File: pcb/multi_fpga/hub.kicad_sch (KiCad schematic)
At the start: 6 parts

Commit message: Fixed with real TXO.
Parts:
- Y1: footprint multi_fpga:TCXO_Can -> multi_fpga:ECS-TXO-5032-122.8-TR
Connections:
- net +3V3: now also Y1.4 (VDD); no longer Y1.1 (VDD), Y1.3 (OE)
- net TCXO_CLK: now also Y1.3 (OUTPUT); no longer Y1.4 (OUT)
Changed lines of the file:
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@@
-	(wire
-		(pts
-			(xy 332.74 185.42) (xy 322.58 185.42)
-		)
-		(stroke
-			(width 0)
-			(type default)
-		)
-	)
 	(wire
 		(pts
@@
 	)
 	(symbol
-		(lib_id "power:+3V3")
-		(at 322.58 185.42 0)
-		(unit 1)
-		(body_style 1)
-		(exclude_from_sim no)
-		(in_bom yes)
-		(on_board yes)
-		(in_pos_files yes)
-		(dnp no)
-		(property "Reference" "#PWR0521"
-			(at 322.58 185.42 0)
-			(hide yes)
-			(show_name no)
-			(do_not_autoplace no)
-			(effects
-				(font
-					(size 1.27 1.27)
-				)
-			)
-		)
-		(property "Value" "+3V3"
-			(at 322.58 185.42 0)
-			(hide yes)
-			(show_name no)
-			(do_not_autoplace no)
-			(effects
-				(font
-					(size 1.27 1.27)
-				)
-			)
-		)
-		(property "Footprint" ""
-			(at 322.58 185.42 0)
-			(hide yes)
-			(show_name no)
-			(do_not_autoplace no)
-			(effects
-				(font
-					(size 1.27 1.27)
-				)
-			)
-		)
-		(property "Datasheet" ""
-			(at 322.58 185.42 0)
-			(hide yes)
-			(show_name no)
-			(do_not_autoplace no)
-			(effects
-				(font
-					(size 1.27 1.27)
-				)
-			)
-		)
-		(property "Description" ""
-			(at 322.58 185.42 0)
-			(hide yes)
-			(show_name no)
-			(do_not_autoplace no)
-			(effects
-				(font
-					(size 1.27 1.27)
-				)
-			)
-		)
-		(pin "1"
-		)
-		(instances
-			(project "hub"
-				(path "/47ab59f9-efc4-4196-ab70-a13d317b89f4"
-					(reference "#PWR0521")
-					(unit 1)
-				)
-			)
-			(project "top"
-				(path "/80f109c4-96c5-4385-bfb6-0f7a96b014ab/a20cffda-dc30-4756-aadc-e7b7a5015c1f"
-					(reference "#PWR0521")
-					(unit 1)
-				)
-			)
-		)
-	)
-	(symbol
 		(lib_id "C")
 		(at 369.57 233.68 0)
@@
 			)
 		)
-		(property "Footprint" "multi_fpga:TCXO_Can"
+		(property "Footprint" "multi_fpga:ECS-TXO-5032-122.8-TR"
 			(at 350.52 184.15 0)
 			(hide yes)

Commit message: Rotated USB-C connector down. Hand-routed. DRC-clean.
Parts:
- A6: footprint multi_fpga:FT232H_Breakout -> multi_fpga:Adafruit_FT232H
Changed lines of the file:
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@@
 			)
 		)
-		(property "Footprint" "multi_fpga:FT232H_Breakout"
+		(property "Footprint" "multi_fpga:Adafruit_FT232H"
 			(at 350.52 294.64 0)
 			(hide yes)

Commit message: Added/cleaned-up power.
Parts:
- added C3: .1uF, SparkFun-Capacitor:C_0603_1608Metric, symbol SparkFun-Capacitor:C
- added C4: 10uF, SparkFun-Capacitor:C_0603_1608Metric_Polar, symbol SparkFun-Capacitor:10uF_0603_6.3V_20%_Polar(Tant)
- added C5: 100uF, SparkFun-Capacitor:Panasonic_D, symbol SparkFun-Capacitor:100uF_6.6x6.6_25V_20%
- added J1: Cluster00_SpokeBus, Connector_PinSocket_2.54mm:PinSocket_2x06_P2.54mm_Vertical, symbol Connector_Generic:Conn_02x06_Odd_Even
- added J2: Cluster01_SpokeBus, Connector_PinSocket_2.54mm:PinSocket_2x06_P2.54mm_Vertical, symbol Connector_Generic:Conn_02x06_Odd_Even
- added J3: Cluster02_SpokeBus, Connector_PinSocket_2.54mm:PinSocket_2x06_P2.54mm_Vertical, symbol Connector_Generic:Conn_02x06_Odd_Even
- added J4: Cluster03_SpokeBus, Connector_PinSocket_2.54mm:PinSocket_2x06_P2.54mm_Vertical, symbol Connector_Generic:Conn_02x06_Odd_Even
- added J5: Cluster00_Power, Connector_PinSocket_2.54mm:PinSocket_1x02_P2.54mm_Vertical, symbol Connector_Generic:Conn_01x02
- added J6: Cluster01_Power, Connector_PinSocket_2.54mm:PinSocket_1x02_P2.54mm_Vertical, symbol Connector_Generic:Conn_01x02
- added J7: Cluster02_Power, Connector_PinSocket_2.54mm:PinSocket_1x02_P2.54mm_Vertical, symbol Connector_Generic:Conn_01x02
- added J8: Cluster03_Power, Connector_PinSocket_2.54mm:PinSocket_1x02_P2.54mm_Vertical, symbol Connector_Generic:Conn_01x02
- added J9: Main Power Input, Connector_JST:JST_XH_B2B-XH-A_1x02_P2.50mm_Vertical, symbol Connector_Generic:Conn_01x02
- C1, C2: value 100nF -> 1uF; footprint (none) -> Capacitor_SMD:C_0201_0603Metric
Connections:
- net +3V3: now also C3.1
- net +5V: now also C4.1, C5.1, J5.1 (Pin_1), J6.1 (Pin_1), J7.1 (Pin_1), J8.1 (Pin_1), J9.1 (Pin_1)
- net GND: now also C3.2, C4.2, C5.2, J1.11 (Pin_11), J1.12 (Pin_12), J1.5 (Pin_5), J1.6 (Pin_6), J2.11 (Pin_11), J2.12 (Pin_12), J2.5 (Pin_5), J2.6 (Pin_6), J3.11 (Pin_11), J3.12 (Pin_12), J3.5 (Pin_5), J3.6 (Pin_6), J4.11 (Pin_11), J4.12 (Pin_12), J4.5 (Pin_5), J4.6 (Pin_6), J5.2 (Pin_2), J6.2 (Pin_2), J7.2 (Pin_2), J8.2 (Pin_2), J9.2 (Pin_2)
- net SPOKE0_CLK: now also J1.10 (Pin_10)
- net SPOKE0_D0: now also J1.1 (Pin_1)
- net SPOKE0_D1: now also J1.2 (Pin_2)
- net SPOKE0_D2: now also J1.3 (Pin_3)
- net SPOKE0_D3: now also J1.4 (Pin_4)
- net SPOKE0_D4: now also J1.7 (Pin_7)
- net SPOKE0_D5: now also J1.8 (Pin_8)
- net SPOKE0_STROBE: now also J1.9 (Pin_9)
- net SPOKE1_CLK: now also J2.10 (Pin_10)
- net SPOKE1_D0: now also J2.1 (Pin_1)
- net SPOKE1_D1: now also J2.2 (Pin_2)
- net SPOKE1_D2: now also J2.3 (Pin_3)
- net SPOKE1_D3: now also J2.4 (Pin_4)
- net SPOKE1_D4: now also J2.7 (Pin_7)
- net SPOKE1_D5: now also J2.8 (Pin_8)
- net SPOKE1_STROBE: now also J2.9 (Pin_9)
- net SPOKE2_CLK: now also J3.10 (Pin_10)
- net SPOKE2_D0: now also J3.1 (Pin_1)
- net SPOKE2_D1: now also J3.2 (Pin_2)
- net SPOKE2_D2: now also J3.3 (Pin_3)
- net SPOKE2_D3: now also J3.4 (Pin_4)
- net SPOKE2_D4: now also J3.7 (Pin_7)
- net SPOKE2_D5: now also J3.8 (Pin_8)
- net SPOKE2_STROBE: now also J3.9 (Pin_9)
- net SPOKE3_CLK: now also J4.10 (Pin_10)
- net SPOKE3_D0: now also J4.1 (Pin_1)
- net SPOKE3_D1: now also J4.2 (Pin_2)
- net SPOKE3_D2: now also J4.3 (Pin_3)
- net SPOKE3_D3: now also J4.4 (Pin_4)
- net SPOKE3_D4: now also J4.7 (Pin_7)
- net SPOKE3_D5: now also J4.8 (Pin_8)
- net SPOKE3_STROBE: now also J4.9 (Pin_9)
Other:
- moved on the sheet: A5, A6, C1, C2, VR5, Y1

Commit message: Fixed library and power issues.
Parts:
- A5: symbol CMOD_A7_35T -> multi_fpga:CMOD_A7_35T
- A6: symbol FT232H_BRK -> multi_fpga:FT232H_BRK
- C1, C2: symbol C -> multi_fpga:C
- VR5: symbol LDO_3V3 -> Regulator_Linear:MCP1700x-330xxTT
- Y1: symbol TCXO_OSC -> multi_fpga:TCXO_OSC
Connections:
- net +3V3: no longer VR5.2 (OUT)
- net +5V: no longer VR5.3 (IN)
- net GND: no longer VR5.1 (GND)
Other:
- moved on the sheet: VR5
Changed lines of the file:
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@@
 	)
 	(symbol
-		(lib_id "C")
+		(lib_id "multi_fpga:C")
 		(at 482.6 146.05 0)
 		(unit 1)
@@
 	)
 	(symbol
-		(lib_id "CMOD_A7_35T")
+		(lib_id "multi_fpga:CMOD_A7_35T")
 		(at 400.05 171.45 0)
 		(unit 1)
@@
 	)
 	(symbol
-		(lib_id "C")
+		(lib_id "multi_fpga:C")
 		(at 497.84 156.21 0)
 		(unit 1)
@@
 	)
 	(symbol
-		(lib_id "TCXO_OSC")
+		(lib_id "multi_fpga:TCXO_OSC")
 		(at 525.78 204.47 0)
 		(unit 1)
@@
 	)
 	(symbol
-		(lib_id "FT232H_BRK")
+		(lib_id "multi_fpga:FT232H_BRK")
 		(at 334.01 345.44 0)
 		(unit 1)
@@
 	)
 	(symbol
-		(lib_id "LDO_3V3")
+		(lib_id "Regulator_Linear:MCP1700x-330xxTT")
 		(at 524.51 139.7 0)
 		(unit 1)
@@
 		)
 	)
-	(embedded_fonts no)
 )

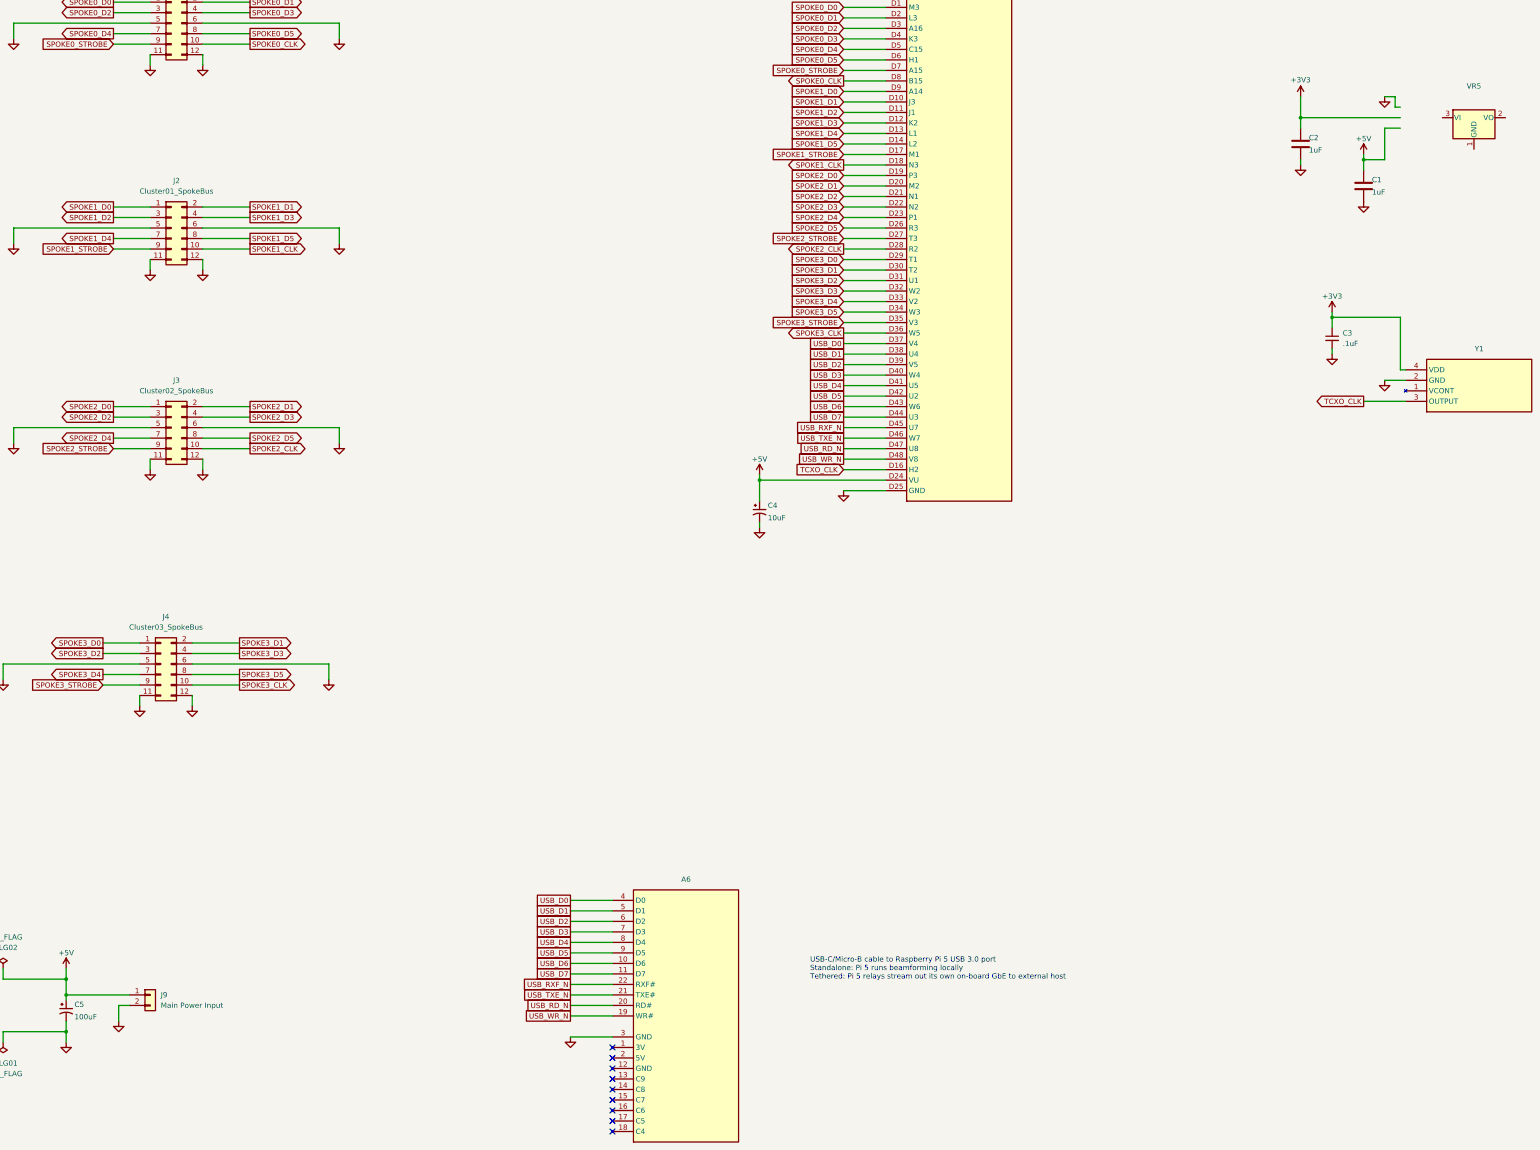
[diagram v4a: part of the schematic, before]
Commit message: Fixed power and C ref des collisions.
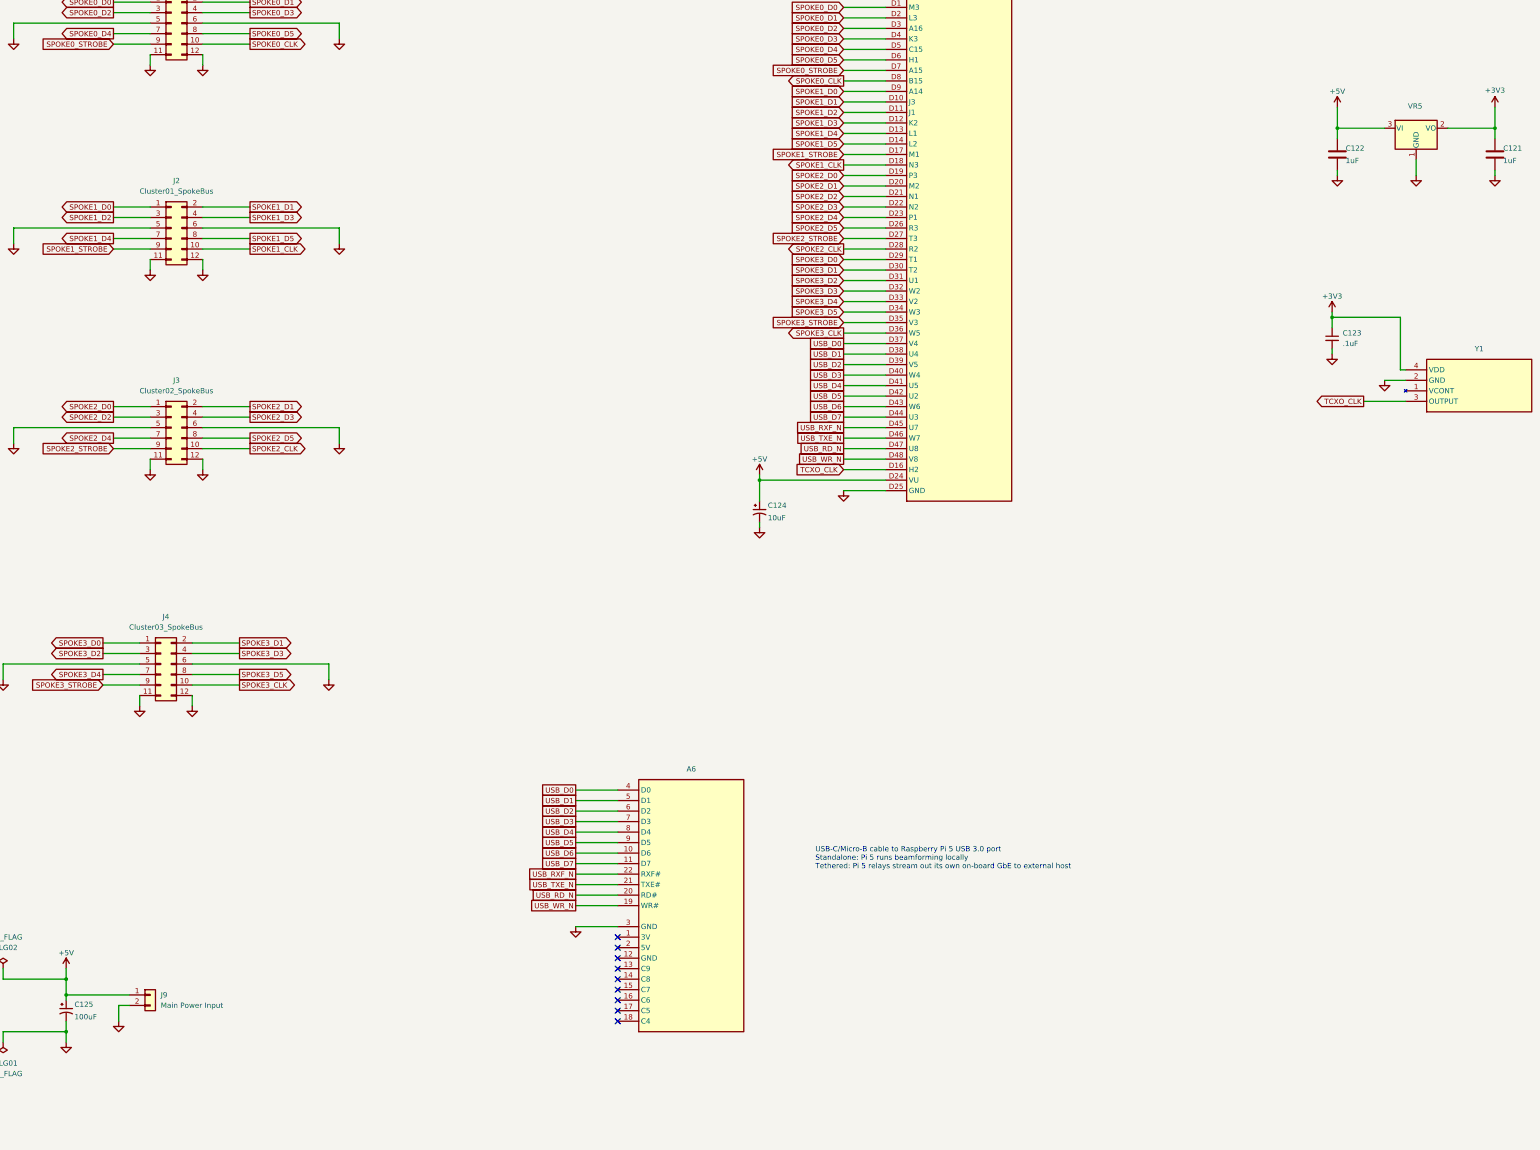
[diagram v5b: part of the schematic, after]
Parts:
- renumbered C2 to C121, C1 to C122, C3 to C123, C4 to C124, C5 to C125
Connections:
- net +3V3: now also VR5.2 (VO)
- net +5V: now also VR5.3 (VI)
- net GND: now also VR5.1 (GND)
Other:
- moved on the sheet: A6, C121, C122, VR5

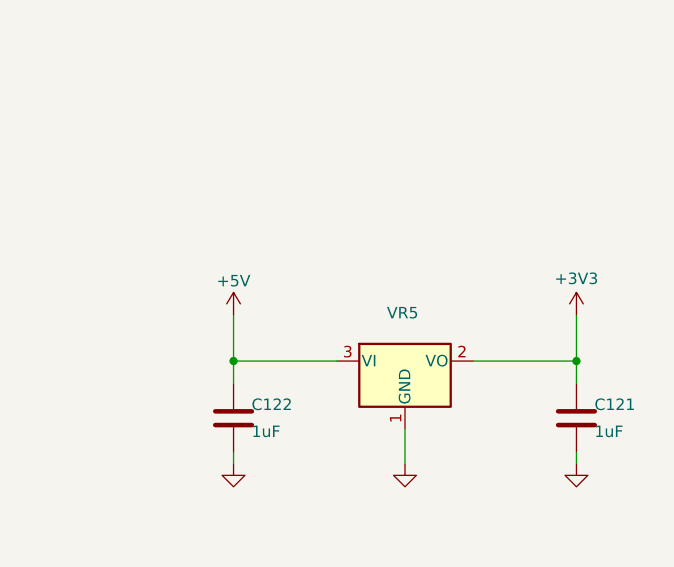
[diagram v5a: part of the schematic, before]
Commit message: Added the LDO regulator part numbers.
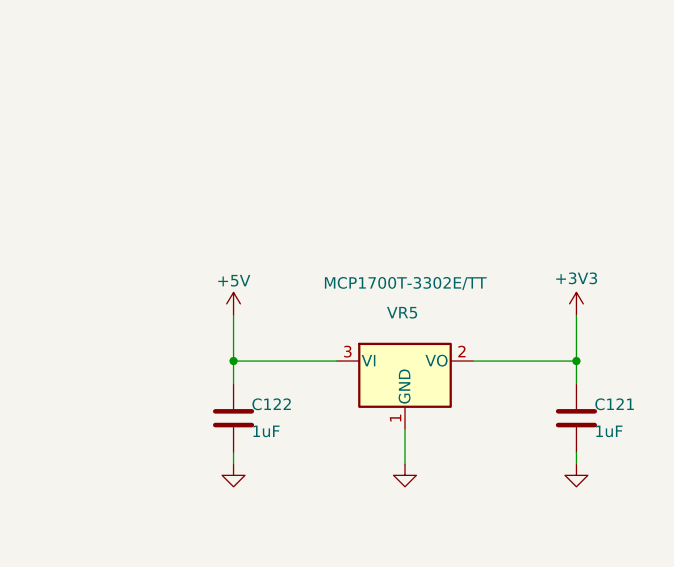
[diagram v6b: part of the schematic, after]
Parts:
- VR5: value (none) -> MCP1700T-3302E/TT
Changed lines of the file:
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@@
 			)
 		)
-		(property "Value" ""
-			(at 510.54 142.24 0)
+		(property "Value" "MCP1700T-3302E/TT"
+			(at 510.54 133.604 0)
 			(show_name no)
 			(do_not_autoplace no)
@@
 		)
 	)
+	(embedded_fonts no)
 )

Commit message: Fixed FPGA module symbols.
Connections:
- net +5V: now also A5.24 (VU); no longer A5.D24 (VU)
- net GND: now also A5.25 (GND); no longer A5.D25 (GND)
- net SPOKE0_CLK: now also A5.8 (PIO08); no longer A5.D8 (B15)
- net SPOKE0_D0: now also A5.1 (PIO01); no longer A5.D1 (M3)
- net SPOKE0_D1: now also A5.2 (PIO02); no longer A5.D2 (L3)
- net SPOKE0_D2: now also A5.3 (PIO03); no longer A5.D3 (A16)
- net SPOKE0_D3: now also A5.4 (PIO04); no longer A5.D4 (K3)
- net SPOKE0_D4: now also A5.5 (PIO05); no longer A5.D5 (C15)
- net SPOKE0_D5: now also A5.6 (PIO06); no longer A5.D6 (H1)
- net SPOKE0_STROBE: now also A5.7 (PIO07); no longer A5.D7 (A15)
- net SPOKE1_CLK: now also A5.16 (AIN16); no longer A5.D18 (N3)
- net SPOKE1_D0: now also A5.9 (PIO09); no longer A5.D9 (A14)
- net SPOKE1_D1: now also A5.10 (PIO10); no longer A5.D10 (J3)
- net SPOKE1_D2: now also A5.11 (PIO11); no longer A5.D11 (J1)
- net SPOKE1_D3: now also A5.12 (PIO12); no longer A5.D12 (K2)
- net SPOKE1_D4: now also A5.13 (PIO13); no longer A5.D13 (L1)
- net SPOKE1_D5: now also A5.14 (PIO14); no longer A5.D14 (L2)
- net SPOKE1_STROBE: now also A5.15 (AIN15); no longer A5.D17 (M1)
- net SPOKE2_CLK: now also A5.26 (PIO26); no longer A5.D28 (R2)
- net SPOKE2_D0: now also A5.17 (PIO17); no longer A5.D19 (P3)
- net SPOKE2_D1: now also A5.18 (PIO18); no longer A5.D20 (M2)
- net SPOKE2_D2: now also A5.19 (PIO19); no longer A5.D21 (N1)
- net SPOKE2_D3: now also A5.20 (PIO20); no longer A5.D22 (N2)
- net SPOKE2_D4: now also A5.21 (PIO21); no longer A5.D23 (P1)
- net SPOKE2_D5: now also A5.22 (PIO22); no longer A5.D26 (R3)
- net SPOKE2_STROBE: now also A5.23 (PIO23); no longer A5.D27 (T3)
- net SPOKE3_CLK: now also A5.34 (PIO34); no longer A5.D36 (W5)
- net SPOKE3_D0: now also A5.27 (PIO27); no longer A5.D29 (T1)
- net SPOKE3_D1: now also A5.28 (PIO28); no longer A5.D30 (T2)
- net SPOKE3_D2: now also A5.29 (PIO29); no longer A5.D31 (U1)
- net SPOKE3_D3: now also A5.30 (PIO30); no longer A5.D32 (W2)
- net SPOKE3_D4: now also A5.31 (PIO31); no longer A5.D33 (V2)
- net SPOKE3_D5: now also A5.32 (PIO32); no longer A5.D34 (W3)
- net SPOKE3_STROBE: now also A5.33 (PIO33); no longer A5.D35 (V3)
- net TCXO_CLK: now also A5.47 (PIO47); no longer A5.D16 (H2)
- net USB_D0: now also A5.35 (PIO35); no longer A5.D37 (V4)
- net USB_D1: now also A5.36 (PIO36); no longer A5.D38 (U4)
- net USB_D2: now also A5.37 (PIO37); no longer A5.D39 (V5)
- net USB_D3: now also A5.38 (PIO38); no longer A5.D40 (W4)
- net USB_D4: now also A5.39 (PIO39); no longer A5.D41 (U5)
- net USB_D5: now also A5.40 (PIO40); no longer A5.D42 (U2)
- net USB_D6: now also A5.41 (PIO41); no longer A5.D43 (W6)
- net USB_D7: now also A5.42 (PIO42); no longer A5.D44 (U3)
- net USB_RD_N: now also A5.45 (PIO45); no longer A5.D47 (U8)
- net USB_RXF_N: now also A5.43 (PIO43); no longer A5.D45 (U7)
- net USB_TXE_N: now also A5.44 (PIO44); no longer A5.D46 (W7)
- net USB_WR_N: now also A5.46 (PIO46); no longer A5.D48 (V8)
- no-connect marks 9 -> 10
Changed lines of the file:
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@@
+	)
+	(no_connect
+		(at 382.27 232.41)
 	)
 	(no_connect

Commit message: Updated FPGA symbols.
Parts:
- C123: Voltage (none) -> 1kV
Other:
- moved on the sheet: A5
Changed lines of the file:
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@@
 			)
 		)
-		(property "Description" ""
+		(property "Description" "100 nF decoupling capacitor, 0402"
 			(at 529.59 148.59 0)
 			(hide yes)
@@
 			)
 		)
-		(property "Description" ""
+		(property "Description" "Hub FPGA module — all 4 spokes + FT232H USB bridge + TCXO clock in (45 signals) on its 48-pin DIP header, no Pmod used; same DIP module form factor as the cluster's Cmod S7, see PHASE4.md, Why all-DIP, no Pmod"
 			(at 400.05 171.45 0)
 			(hide yes)
@@
 			)
 		)
-		(pin "D1"
+		(pin "33"
 		)
-		(pin "D2"
+		(pin "42"
 		)
-		(pin "D3"
+		(pin "43"
 		)
-		(pin "D4"
+		(pin "11"
 		)
-		(pin "D5"
+		(pin "12"
 		)
-		(pin "D6"
+		(pin "13"
 		)
-		(pin "D7"
+		(pin "24"
 		)
-		(pin "D8"
+		(pin "25"
 		)
-		(pin "D9"
+		(pin "1"
 		)
-		(pin "D10"
+		(pin "34"
 		)
-		(pin "D11"
+		(pin "26"
 		)
-		(pin "D12"
+		(pin "27"
 		)
-		(pin "D13"
+		(pin "39"
 		)
-		(pin "D14"
+		(pin "40"
 		)
-		(pin "D17"
+		(pin "41"
 		)
-		(pin "D18"
+		(pin "37"
 		)
-		(pin "D19"
+		(pin "17"
 		)
-		(pin "D20"
+		(pin "18"
 		)
-		(pin "D21"
+		(pin "47"
 		)
-		(pin "D22"
+		(pin "48"
 		)
-		(pin "D23"
+		(pin "44"
 		)
-		(pin "D26"
+		(pin "45"
 		)
-		(pin "D27"
+		(pin "46"
 		)
-		(pin "D28"
+		(pin "29"
 		)
-		(pin "D29"
+		(pin "30"
 		)
-		(pin "D30"
+		(pin "31"
 		)
-		(pin "D31"
+		(pin "32"
 		)
-		(pin "D32"
+		(pin "21"
 		)
-		(pin "D33"
+		(pin "22"
 		)
-		(pin "D34"
+		(pin "38"
 		)
-		(pin "D35"
+		(pin "4"
 		)
-		(pin "D36"
+		(pin "5"
 		)
-		(pin "D37"
+		(pin "6"
 		)
-		(pin "D38"
+		(pin "7"
 		)
-		(pin "D39"
+		(pin "35"
 		)
-		(pin "D40"
+		(pin "36"
 		)
-		(pin "D41"
+		(pin "14"
 		)
-		(pin "D42"
+		(pin "15"
+		)
+		(pin "16"
 		)
-		(pin "D43"
+		(pin "2"
 		)
-		(pin "D44"
+		(pin "3"
 		)
-		(pin "D45"
+		(pin "23"
 		)
-		(pin "D46"
+		(pin "28"
 		)
-		(pin "D47"
+		(pin "8"
 		)
-		(pin "D48"
+		(pin "9"
 		)
-		(pin "D16"
+		(pin "19"
 		)
-		(pin "D24"
+		(pin "20"
 		)
-		(pin "D25"
+		(pin "10"
 		)
 		(instances
@@
 			)
 		)
-		(property "Description" ""
+		(property "Description" "100 nF decoupling capacitor, 0402"
 			(at 491.49 148.59 0)
 			(hide yes)
@@
 			)
 		)
-		(property "Datasheet" ""
+		(property "Datasheet" "https://ecsxtal.com/store/pdf/ECS-TXO-5032.pdf"
 			(at 525.78 204.47 0)
 			(hide yes)
@@
 			)
 		)
-		(property "Description" ""
+		(property "Description" "Master clock; ECS-TXO-5032-122.8-TR, 12.288 MHz HCMOS TCXO, +-2.5ppm, 3.3V. Pin 1 is N/C on this plain-TXO variant (VCONT is only active on the ECS-VTXO-5032 VC-TCXO option)."
 			(at 525.78 204.47 0)
 			(hide yes)
@@
 			)
 		)
-		(property "Description" ""
+		(property "Description" "USB 2.0 Hi-Speed synchronous 245-mode FIFO bridge to Raspberry Pi 5 USB 3.0 port (device is USB2-speed, ~320 Mbps, backward compatible); self-powered over its own USB-C cable to the RPi5, not from the hub -- only the 13 FT245 sync-FIFO signal pins are wired here, the other 9 (3V out, 5V in, 2nd GND, C4-C9) are real pads on the new 2x11 board but intentionally unconnected"
 			(at 335.28 318.77 0)
 			(hide yes)
@@
 			)
 		)
-		(property "Voltage" ""
+		(property "Voltage" "1kV"
 			(at 492.76 194.3162 0)
 			(hide yes)
@@
 			)
 		)
-		(property "Datasheet" ""
+		(property "Datasheet" "http://ww1.microchip.com/downloads/en/DeviceDoc/20001826D.pdf"
 			(at 510.54 142.24 0)
 			(hide yes)
@@
 			)
 		)
-		(property "Description" ""
+		(property "Description" "250mA Low Quiscent Current LDO, 3.3V output, SOT-23"
 			(at 510.54 142.24 0)
 			(hide yes)
